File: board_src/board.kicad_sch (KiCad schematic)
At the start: 16 parts, among them J1 Conn_01x05, J16 Conn_01x05, J17 Conn_01x05, J18 Conn_02x20_Counter_Clockwise, J2 Conn_01x05, J20 Conn_02x20_Counter_Clockwise, J21 Conn_02x20_Counter_Clockwise, J22 Conn_02x20_Counter_Clockwise, J26 Conn_01x20_Socket, J28 Conn_01x20_Socket, J30 Conn_01x05, J31 Conn_01x05, U1 Pico, U4 Pico

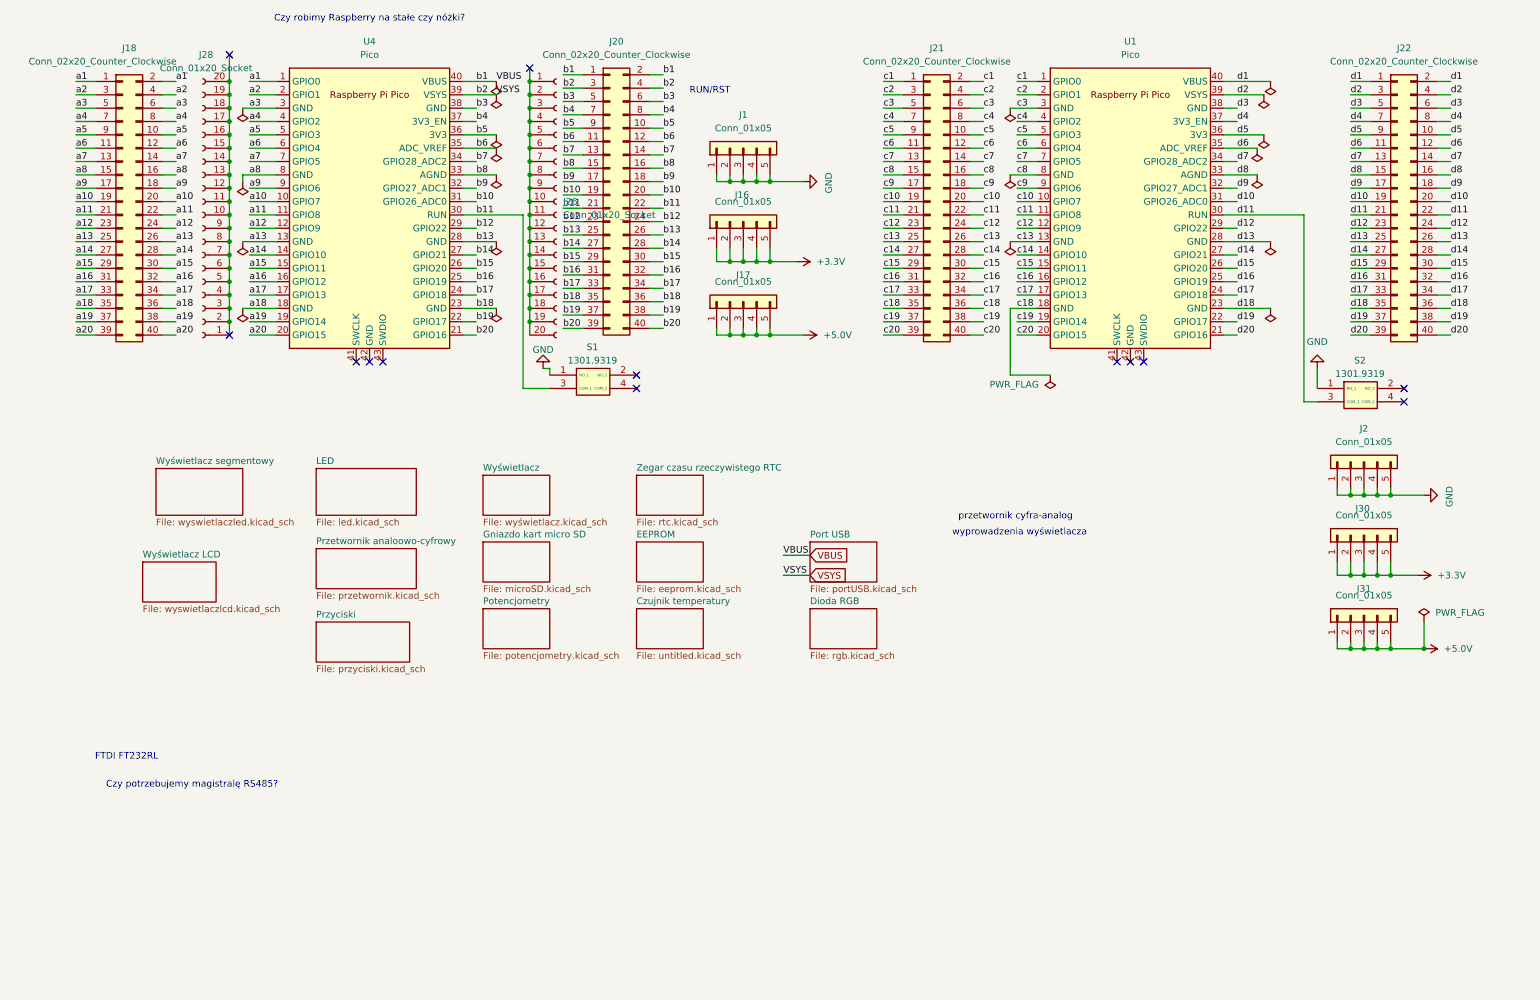
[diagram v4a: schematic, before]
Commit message: Wersja ze sciezkami miedzianymi
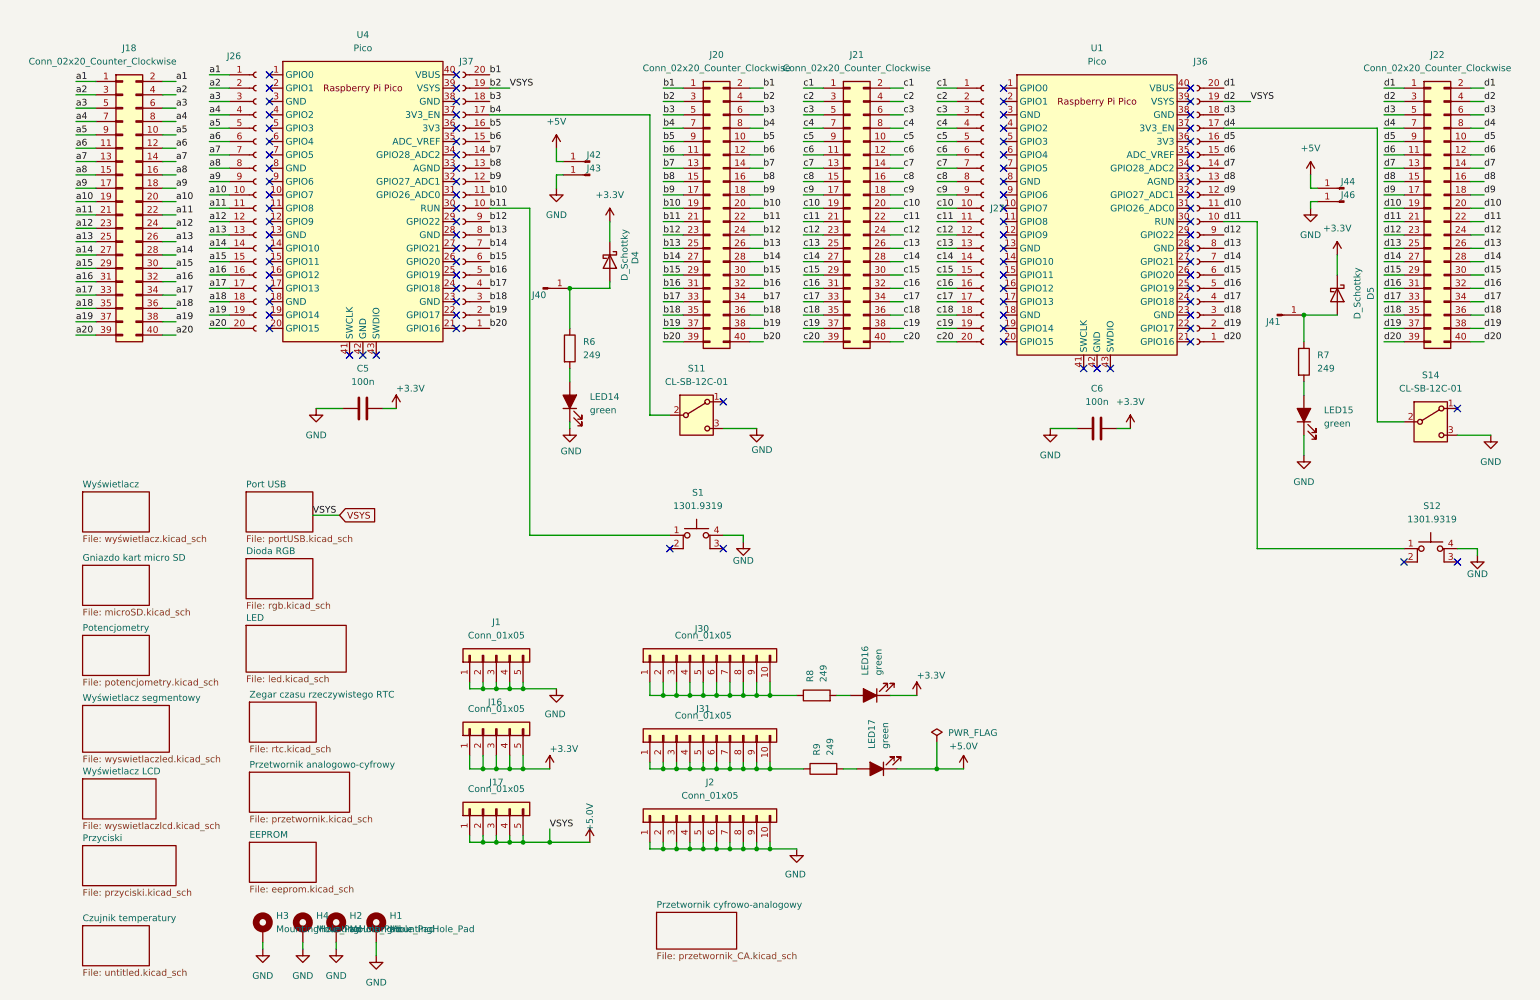
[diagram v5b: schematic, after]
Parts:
- removed J28: Conn_01x20_Socket, symbol Connector:Conn_01x20_Socket
- removed S2: 1301.9319, footprints:przycisk, symbol przycisk:1301.9319
- added C5, C6: 100n, Capacitor_SMD:C_0603_1608Metric, symbol Device:C
- added D4, D5: D_Schottky, Diode_SMD:D_SMA, symbol Device:D_Schottky
- added H1, H2, H3, H4: MountingHole_Pad, MountingHole:MountingHole_3.2mm_M3_DIN965_Pad_TopBottom, symbol Mechanical:MountingHole_Pad
- added J27, J36, J37: Conn_01x20_Socket, Connector_PinSocket_2.54mm:PinSocket_1x20_P2.54mm_Vertical, symbol Connector:Conn_01x20_Socket
- added J40, J41, J42, J43, J44, J46: Conn_01x01_Pin, Connector_PinHeader_2.54mm:PinHeader_1x01_P2.54mm_Vertical, symbol Connector:Conn_01x01_Pin
- added LED14, LED15, LED16, LED17: green, footprints:LEDC1608X100N, symbol Device:LED_Filled
- added R6, R7, R8, R9: 249, Resistor_SMD:R_0603_1608Metric, symbol Device:R
- added S11, S14: CL-SB-12C-01, footprints:CLSB12C01, symbol Switch:SW_SPDT
- added S12: 1301.9319, Button_Switch_THT:SW_PUSH_6mm_H9.5mm, symbol Switch:SW_MEC_5E
- J2, J30, J31: footprint Connector_PinHeader_2.54mm:PinHeader_1x05_P2.54mm_Vertical -> Connector_PinHeader_2.54mm:PinHeader_1x10_P2.54mm_Vertical; symbol Connector_Generic:Conn_01x05 -> Connector_Generic:Conn_01x10
- J26: footprint (none) -> Connector_PinSocket_2.54mm:PinSocket_1x20_P2.54mm_Vertical
- S1: footprint footprints:przycisk -> Button_Switch_THT:SW_PUSH_6mm_H9.5mm; symbol przycisk:1301.9319 -> Switch:SW_MEC_5E
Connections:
- net +3.3V: now also C5.2, C6.2, D4.1 (K), D5.1 (K), LED16.1 (K); no longer J30.1 (Pin_1), J30.2 (Pin_2), J30.3 (Pin_3), J30.4 (Pin_4), J30.5 (Pin_5)
- net +5.0V: now also J20.3 (Pin_3), J20.4 (Pin_4), J22.3 (Pin_3), J22.4 (Pin_4), J36.19 (Pin_19), J37.19 (Pin_19), LED17.1 (K); no longer J31.1 (Pin_1), J31.2 (Pin_2), J31.3 (Pin_3), J31.4 (Pin_4), J31.5 (Pin_5)
- net GND: now also J2.10 (Pin_10), J2.6 (Pin_6), J2.7 (Pin_7), J2.8 (Pin_8), J2.9 (Pin_9), S1.4 (A), C5.1, C6.1, H1.1, H2.1, H3.1, H4.1, J43.1 (Pin_1), J46.1 (Pin_1), LED14.1 (K), LED15.1 (K), S11.3 (C), S12.4 (A), S14.3 (C); no longer S1.1 (NO_1)
- net a1: now also J26.1 (Pin_1); no longer U4.1 (GPIO0)
- net a10: now also J26.10 (Pin_10); no longer U4.10 (GPIO7)
- net a11: now also J26.11 (Pin_11); no longer U4.11 (GPIO8)
- net a12: now also J26.12 (Pin_12); no longer U4.12 (GPIO9)
- net a13: now also J26.13 (Pin_13); no longer U4.13 (GND)
- net a14: now also J26.14 (Pin_14); no longer U4.14 (GPIO10)
- net a15: now also J26.15 (Pin_15); no longer U4.15 (GPIO11)
- net a16: now also J26.16 (Pin_16); no longer U4.16 (GPIO12)
- net a17: now also J26.17 (Pin_17); no longer U4.17 (GPIO13)
- net a18: now also J26.18 (Pin_18); no longer U4.18 (GND)
- net a19: now also J26.19 (Pin_19); no longer U4.19 (GPIO14)
- net a2: now also J26.2 (Pin_2); no longer U4.2 (GPIO1)
- net a20: now also J26.20 (Pin_20); no longer U4.20 (GPIO15)
- net a3: now also J26.3 (Pin_3); no longer U4.3 (GND)
- net a4: now also J26.4 (Pin_4); no longer U4.4 (GPIO2)
- net a5: now also J26.5 (Pin_5); no longer U4.5 (GPIO3)
- net a6: now also J26.6 (Pin_6); no longer U4.6 (GPIO4)
- net a7: now also J26.7 (Pin_7); no longer U4.7 (GPIO5)
- net a8: now also J26.8 (Pin_8); no longer U4.8 (GND)
- net a9: now also J26.9 (Pin_9); no longer U4.9 (GPIO6)
- net b10: now also J37.11 (Pin_11); no longer U4.31 (GPIO26_ADC0)
- net b11: now also S1.1, J37.10 (Pin_10); no longer S1.3 (COM_1), U4.30 (RUN)
- net b12: now also J37.9 (Pin_9); no longer U4.29 (GPIO22)
- net b13: now also J37.8 (Pin_8); no longer U4.28 (GND)
- net b14: now also J37.7 (Pin_7); no longer U4.27 (GPIO21)
- net b15: now also J37.6 (Pin_6); no longer U4.26 (GPIO20)
- net b16: now also J37.5 (Pin_5); no longer U4.25 (GPIO19)
- net b17: now also J37.4 (Pin_4); no longer U4.24 (GPIO18)
- net b18: now also J37.3 (Pin_3); no longer U4.23 (GND)
- net b19: now also J37.2 (Pin_2); no longer U4.22 (GPIO17)
- net b20: now also J37.1 (Pin_1); no longer U4.21 (GPIO16)
- net b3: now also J37.18 (Pin_18); no longer U4.38 (GND)
- net b4: now also J37.17 (Pin_17), S11.2 (B); no longer U4.37 (3V3_EN)
- net b5: now also J37.16 (Pin_16); no longer U4.36 (3V3)
- net b6: now also J37.15 (Pin_15); no longer U4.35 (ADC_VREF)
- net b7: now also J37.14 (Pin_14); no longer U4.34 (GPIO28_ADC2)
- net b8: now also J37.13 (Pin_13); no longer U4.33 (AGND)
- net b9: now also J37.12 (Pin_12); no longer U4.32 (GPIO27_ADC1)
- net c1: now also J27.1 (Pin_1); no longer U1.1 (GPIO0)
- net c10: now also J27.10 (Pin_10); no longer U1.10 (GPIO7)
- net c11: now also J27.11 (Pin_11); no longer U1.11 (GPIO8)
- net c12: now also J27.12 (Pin_12); no longer U1.12 (GPIO9)
- net c13: now also J27.13 (Pin_13); no longer U1.13 (GND)
- net c14: now also J27.14 (Pin_14); no longer U1.14 (GPIO10)
- net c15: now also J27.15 (Pin_15); no longer U1.15 (GPIO11)
- net c16: now also J27.16 (Pin_16); no longer U1.16 (GPIO12)
- net c17: now also J27.17 (Pin_17); no longer U1.17 (GPIO13)
- net c18: now also J27.18 (Pin_18); no longer U1.18 (GND)
- net c19: now also J27.19 (Pin_19); no longer U1.19 (GPIO14)
- net c2: now also J27.2 (Pin_2); no longer U1.2 (GPIO1)
- net c20: now also J27.20 (Pin_20); no longer U1.20 (GPIO15)
- net c3: now also J27.3 (Pin_3); no longer U1.3 (GND)
- net c4: now also J27.4 (Pin_4); no longer U1.4 (GPIO2)
- net c5: now also J27.5 (Pin_5); no longer U1.5 (GPIO3)
- net c6: now also J27.6 (Pin_6); no longer U1.6 (GPIO4)
- net c7: now also J27.7 (Pin_7); no longer U1.7 (GPIO5)
- net c8: now also J27.8 (Pin_8); no longer U1.8 (GND)
- net c9: now also J27.9 (Pin_9); no longer U1.9 (GPIO6)
- net d1: now also J36.20 (Pin_20); no longer U1.40 (VBUS)
- net d10: now also J36.11 (Pin_11); no longer U1.31 (GPIO26_ADC0)
- net d11: now also J36.10 (Pin_10), S12.1; no longer U1.30 (RUN)
- net d12: now also J36.9 (Pin_9); no longer U1.29 (GPIO22)
- net d13: now also J36.8 (Pin_8); no longer U1.28 (GND)
- net d14: now also J36.7 (Pin_7); no longer U1.27 (GPIO21)
- net d15: now also J36.6 (Pin_6); no longer U1.26 (GPIO20)
- net d16: now also J36.5 (Pin_5); no longer U1.25 (GPIO19)
- net d17: now also J36.4 (Pin_4); no longer U1.24 (GPIO18)
- net d18: now also J36.3 (Pin_3); no longer U1.23 (GND)
- net d19: now also J36.2 (Pin_2); no longer U1.22 (GPIO17)
- net d20: now also J36.1 (Pin_1); no longer U1.21 (GPIO16)
- net d3: now also J36.18 (Pin_18); no longer U1.38 (GND)
- net d4: now also J36.17 (Pin_17), S14.2 (B); no longer U1.37 (3V3_EN)
- net d5: now also J36.16 (Pin_16); no longer U1.36 (3V3)
- net d6: now also J36.15 (Pin_15); no longer U1.35 (ADC_VREF)
- net d7: now also J36.14 (Pin_14); no longer U1.34 (GPIO28_ADC2)
- net d8: now also J36.13 (Pin_13); no longer U1.33 (AGND)
- net d9: now also J36.12 (Pin_12); no longer U1.32 (GPIO27_ADC1)
- net VBUS renamed b1
- net b1: now also J37.20 (Pin_20); no longer U4.40 (VBUS)
- removed net VSYS: J20.3 (Pin_3), J20.4 (Pin_4), U4.39 (VSYS)
- removed net d2: J22.3 (Pin_3), J22.4 (Pin_4), U1.39 (VSYS)
- new net: D4.2 (A), J40.1 (Pin_1), R6.1
- new net: LED14.2 (A), R6.2
- new net: LED15.2 (A), R7.2
- new net: LED17.2 (A), R9.2
- new net: J31.1 (Pin_1), J31.10 (Pin_10), J31.2 (Pin_2), J31.3 (Pin_3), J31.4 (Pin_4), J31.5 (Pin_5), J31.6 (Pin_6), J31.7 (Pin_7), J31.8 (Pin_8), J31.9 (Pin_9), R9.1
- new net: J30.1 (Pin_1), J30.10 (Pin_10), J30.2 (Pin_2), J30.3 (Pin_3), J30.4 (Pin_4), J30.5 (Pin_5), J30.6 (Pin_6), J30.7 (Pin_7), J30.8 (Pin_8), J30.9 (Pin_9), R8.1
- new net: D5.2 (A), J41.1 (Pin_1), R7.1
- new net: LED16.2 (A), R8.2
- new net +5V: J42.1 (Pin_1), J44.1 (Pin_1)
- no-connect marks 13 -> 92
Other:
- sheet Przetwornik analoowo-cyfrowy renamed Przetwornik analogowo-cyfrowy
- added sheet Przetwornik cyfrowo-analogowy (przetwornik_CA.kicad_sch)
- note removed: "Czy potrzebujemy magistralę RS485?"
- note removed: "Czy robimy Raspberry na stałe czy nóżki?"
- note removed: "FTDI FT232RL"
- note removed: "RUN/RST"
- note removed: "przetwornik cyfra-analog"
- note removed: "wyprowadzenia wyświetlacza"
- moved on the sheet: J1, J16, J17, J20, J21, J22, J26, S1, U1, U4

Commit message: sciezki polaczen
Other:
- moved on the sheet: H1, H2, H3, H4
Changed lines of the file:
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@@
 	(wire
 		(pts
-			(xy 69.85 184.15) (xy 69.85 186.69)
+			(xy 240.03 151.13) (xy 240.03 152.4)
 		)
 		(stroke
@@
 	(wire
 		(pts
-			(xy 62.23 184.15) (xy 62.23 185.42)
+			(xy 232.41 151.13) (xy 232.41 152.4)
 		)
 		(stroke
@@
 	(wire
 		(pts
-			(xy 55.88 184.15) (xy 55.88 185.42)
+			(xy 226.06 151.13) (xy 226.06 152.4)
 		)
 		(stroke
@@
 	(wire
 		(pts
-			(xy 48.26 184.15) (xy 48.26 185.42)
+			(xy 218.44 151.13) (xy 218.44 152.4)
 		)
 		(stroke
@@
 	(symbol
 		(lib_id "Mechanical:MountingHole_Pad")
-		(at 62.23 181.61 0)
+		(at 232.41 148.59 0)
 		(unit 1)
 		(exclude_from_sim yes)
@@
 		(fields_autoplaced yes)
 		(property "Reference" "H2"
-			(at 64.77 179.0699 0)
+			(at 234.95 146.0499 0)
 			(effects
 				(font
@@
 		)
 		(property "Value" "MountingHole_Pad"
-			(at 64.77 181.6099 0)
+			(at 234.95 148.5899 0)
 			(effects
 				(font
@@
 		)
 		(property "Footprint" "MountingHole:MountingHole_3.2mm_M3_DIN965_Pad_TopBottom"
-			(at 62.23 181.61 0)
+			(at 232.41 148.59 0)
 			(effects
 				(font
@@
 		)
 		(property "Datasheet" "~"
-			(at 62.23 181.61 0)
+			(at 232.41 148.59 0)
 			(effects
 				(font
@@
 		)
 		(property "Description" "Mounting Hole with connection"
-			(at 62.23 181.61 0)
+			(at 232.41 148.59 0)
 			(effects
 				(font
@@
 	(symbol
 		(lib_id "Mechanical:MountingHole_Pad")
-		(at 69.85 181.61 0)
+		(at 240.03 148.59 0)
 		(unit 1)
 		(exclude_from_sim yes)
@@
 		(fields_autoplaced yes)
 		(property "Reference" "H1"
-			(at 72.39 179.0699 0)
+			(at 242.57 146.0499 0)
 			(effects
 				(font
@@
 		)
 		(property "Value" "MountingHole_Pad"
-			(at 72.39 181.6099 0)
+			(at 242.57 148.5899 0)
 			(effects
 				(font
@@
 		)
 		(property "Footprint" "MountingHole:MountingHole_3.2mm_M3_DIN965_Pad_TopBottom"
-			(at 69.85 181.61 0)
+			(at 240.03 148.59 0)
 			(effects
 				(font
@@
 		)
 		(property "Datasheet" "~"
-			(at 69.85 181.61 0)
+			(at 240.03 148.59 0)
 			(effects
 				(font
@@
 		)
 		(property "Description" "Mounting Hole with connection"
-			(at 69.85 181.61 0)
+			(at 240.03 148.59 0)
 			(effects
 				(font
@@
 	(symbol
 		(lib_id "Mechanical:MountingHole_Pad")
-		(at 55.88 181.61 0)
+		(at 226.06 148.59 0)
 		(unit 1)
 		(exclude_from_sim yes)
@@
 		(fields_autoplaced yes)
 		(property "Reference" "H4"
-			(at 58.42 179.0699 0)
+			(at 228.6 146.0499 0)
 			(effects
 				(font
@@
 		)
 		(property "Value" "MountingHole_Pad"
-			(at 58.42 181.6099 0)
+			(at 228.6 148.5899 0)
 			(effects
 				(font
@@
 		)
 		(property "Footprint" "MountingHole:MountingHole_3.2mm_M3_DIN965_Pad_TopBottom"
-			(at 55.88 181.61 0)
+			(at 226.06 148.59 0)
 			(effects
 				(font
@@
 		)
 		(property "Datasheet" "~"
-			(at 55.88 181.61 0)
+			(at 226.06 148.59 0)
 			(effects
 				(font
@@
 		)
 		(property "Description" "Mounting Hole with connection"
-			(at 55.88 181.61 0)
+			(at 226.06 148.59 0)
 			(effects
 				(font
@@
 	(symbol
 		(lib_id "Mechanical:MountingHole_Pad")
-		(at 48.26 181.61 0)
+		(at 218.44 148.59 0)
 		(unit 1)
 		(exclude_from_sim yes)
@@
 		(fields_autoplaced yes)
 		(property "Reference" "H3"
-			(at 50.8 179.0699 0)
+			(at 220.98 146.0499 0)
 			(effects
 				(font
@@
 		)
 		(property "Value" "MountingHole_Pad"
-			(at 50.8 181.6099 0)
+			(at 220.98 148.5899 0)
 			(effects
 				(font
@@
 		)
 		(property "Footprint" "MountingHole:MountingHole_3.2mm_M3_DIN965_Pad_TopBottom"
-			(at 48.26 181.61 0)
+			(at 218.44 148.59 0)
 			(effects
 				(font
@@
 		)
 		(property "Datasheet" "~"
-			(at 48.26 181.61 0)
+			(at 218.44 148.59 0)
 			(effects
 				(font
@@
 		)
 		(property "Description" "Mounting Hole with connection"
-			(at 48.26 181.61 0)
+			(at 218.44 148.59 0)
 			(effects
 				(font
@@
 	(symbol
 		(lib_id "power:GND")
-		(at 55.88 185.42 0)
+		(at 226.06 152.4 0)
 		(unit 1)
 		(exclude_from_sim no)
@@
 		(fields_autoplaced yes)
 		(property "Reference" "#PWR067"
-			(at 55.88 191.77 0)
+			(at 226.06 158.75 0)
 			(effects
 				(font
@@
 		)
 		(property "Value" "GND"
-			(at 55.88 190.5 0)
+			(at 226.06 157.48 0)
 			(effects
 				(font
@@
 		)
 		(property "Footprint" ""
-			(at 55.88 185.42 0)
+			(at 226.06 152.4 0)
 			(effects
 				(font
@@
 		)
 		(property "Datasheet" ""
-			(at 55.88 185.42 0)
+			(at 226.06 152.4 0)
 			(effects
 				(font
@@
 		)
 		(property "Description" "Power symbol creates a global label with name \"GND\" , ground"
-			(at 55.88 185.42 0)
+			(at 226.06 152.4 0)
 			(effects
 				(font
@@
 	(symbol
 		(lib_id "power:GND")
-		(at 48.26 185.42 0)
+		(at 218.44 152.4 0)
 		(unit 1)
 		(exclude_from_sim no)
@@
 		(fields_autoplaced yes)
 		(property "Reference" "#PWR066"
-			(at 48.26 191.77 0)
+			(at 218.44 158.75 0)
 			(effects
 				(font
@@
 		)
 		(property "Value" "GND"
-			(at 48.26 190.5 0)
+			(at 218.44 157.48 0)
 			(effects
 				(font
@@
 		)
 		(property "Footprint" ""
-			(at 48.26 185.42 0)
+			(at 218.44 152.4 0)
 			(effects
 				(font
@@
 		)
 		(property "Datasheet" ""
-			(at 48.26 185.42 0)
+			(at 218.44 152.4 0)
 			(effects
 				(font
@@
 		)
 		(property "Description" "Power symbol creates a global label with name \"GND\" , ground"
-			(at 48.26 185.42 0)
+			(at 218.44 152.4 0)
 			(effects
 				(font
@@
 	(symbol
 		(lib_id "power:GND")
-		(at 62.23 185.42 0)
+		(at 232.41 152.4 0)
 		(unit 1)
 		(exclude_from_sim no)
@@
 		(fields_autoplaced yes)
 		(property "Reference" "#PWR065"
-			(at 62.23 191.77 0)
+			(at 232.41 158.75 0)
 			(effects
 				(font
@@
 		)
 		(property "Value" "GND"
-			(at 62.23 190.5 0)
+			(at 232.41 157.48 0)
 			(effects
 				(font
@@
 		)
 		(property "Footprint" ""
-			(at 62.23 185.42 0)
+			(at 232.41 152.4 0)
 			(effects
 				(font
@@
 		)
 		(property "Datasheet" ""
-			(at 62.23 185.42 0)
+			(at 232.41 152.4 0)
 			(effects
 				(font
@@
 		)
 		(property "Description" "Power symbol creates a global label with name \"GND\" , ground"
-			(at 62.23 185.42 0)
+			(at 232.41 152.4 0)
 			(effects
 				(font
@@
 	(symbol
 		(lib_id "power:GND")
-		(at 69.85 186.69 0)
+		(at 240.03 152.4 0)
 		(unit 1)
 		(exclude_from_sim no)
@@
 		(fields_autoplaced yes)
 		(property "Reference" "#PWR064"
-			(at 69.85 193.04 0)
+			(at 240.03 158.75 0)
 			(effects
 				(font
@@
 		)
 		(property "Value" "GND"
-			(at 69.85 191.77 0)
+			(at 240.03 157.48 0)
 			(effects
 				(font
@@
 		)
 		(property "Footprint" ""
-			(at 69.85 186.69 0)
+			(at 240.03 152.4 0)
 			(effects
 				(font
@@
 		)
 		(property "Datasheet" ""
-			(at 69.85 186.69 0)
+			(at 240.03 152.4 0)
 			(effects
 				(font
@@
 		)
 		(property "Description" "Power symbol creates a global label with name \"GND\" , ground"
-			(at 69.85 186.69 0)
+			(at 240.03 152.4 0)
 			(effects
 				(font
@@
 	)
 	(sheet
-		(at 123.19 178.435)
+		(at 45.72 180.34)
 		(size 15.24 6.985)
 		(exclude_from_sim no)
@@
 		)
 		(property "Sheetname" "Przetwornik cyfrowo-analogowy"
-			(at 123.19 177.7234 0)
+			(at 45.72 179.6284 0)
 			(effects
 				(font
@@
 		)
 		(property "Sheetfile" "przetwornik_CA.kicad_sch"
-			(at 123.19 186.0046 0)
+			(at 45.72 187.9096 0)
 			(effects
 				(font
